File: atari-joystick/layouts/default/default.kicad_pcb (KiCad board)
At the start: 2 copper layers, 31.5 x 30 mm, 19 parts

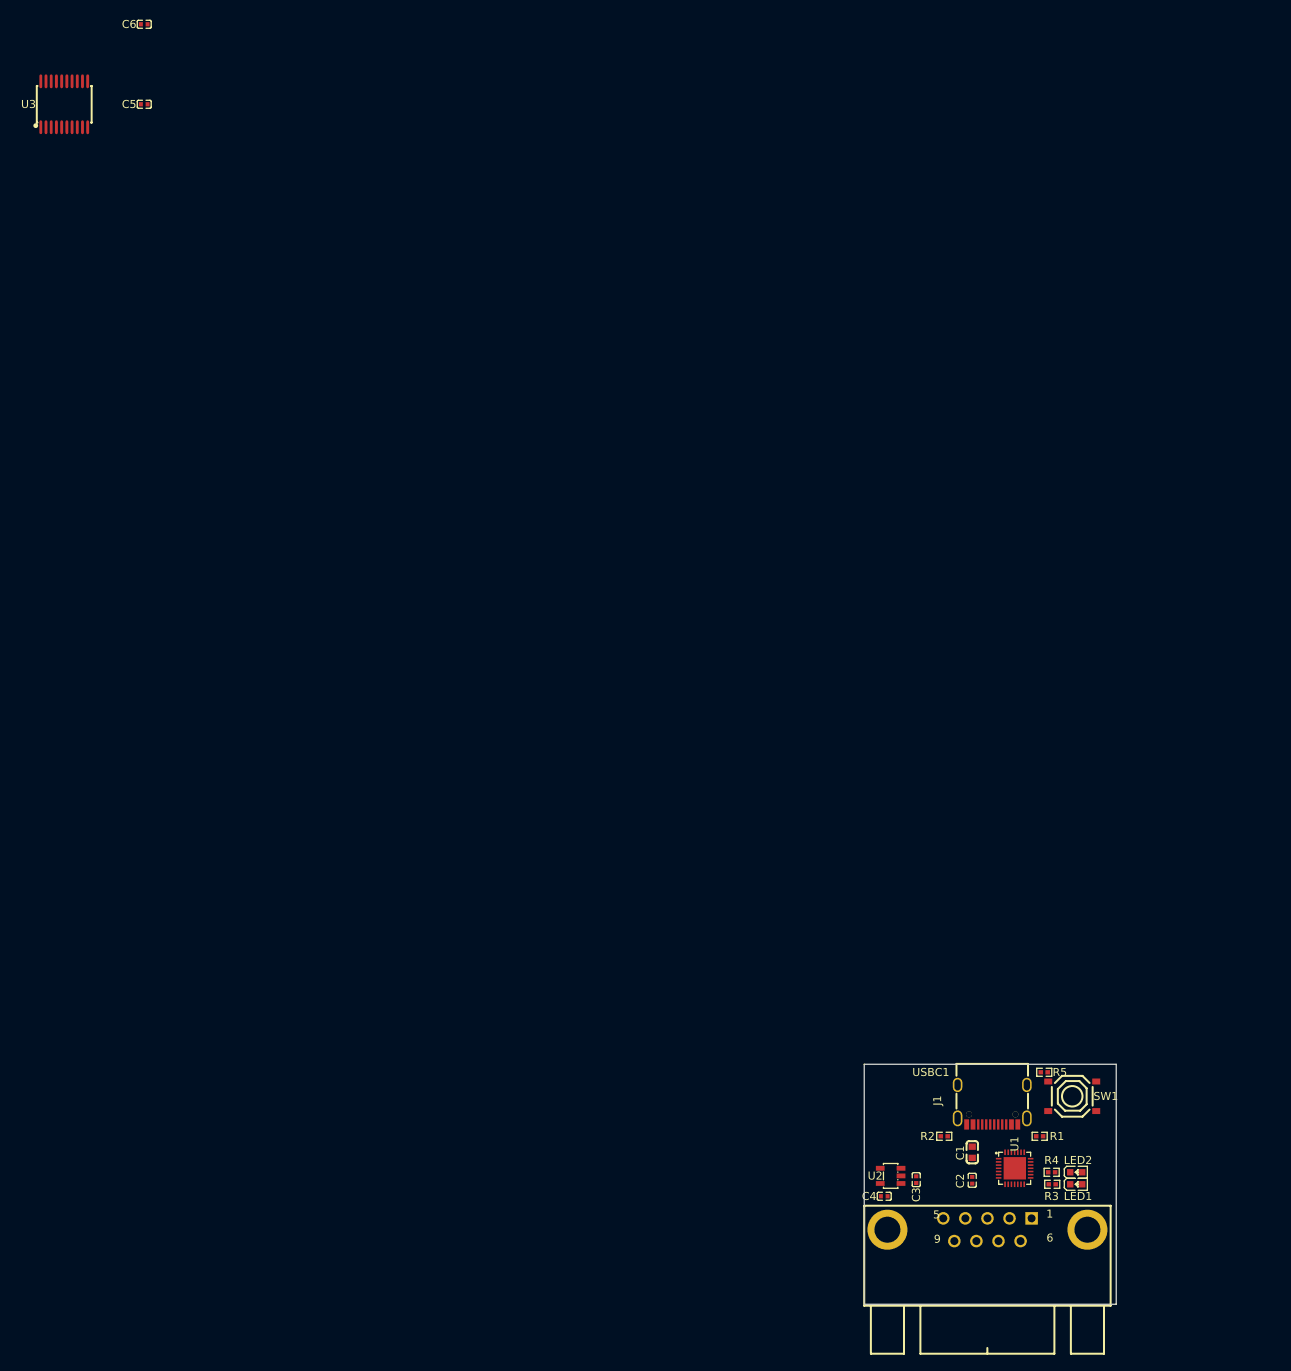
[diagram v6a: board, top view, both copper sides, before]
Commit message: atari-joystick: x68000-keyboard の改修を取り込み (LED 削除 / SW / フットプリント)
x68000-keyboard と同じ方針でジョイスティック基板も以下に揃える:

- デバッグ LED (LED0/LED1) と直列抵抗を削除。PB11 / PB12 は未使用化
- BOOT ボタンを XKB TS-1187A (4 ピン 5.1×5.1mm) から
  XUNPU TS-1088-AR02016 (2 ピン 3.9×3.0mm) に変更
- USB-C コネクタのシルク線幅を 0.25mm → 0.2mm に調整 (DRC 対応)
- TC7MPB9307FT (TSSOP-20) フットプリント整形
- buttons.ato に TactSwitch_2P モジュール追加

SW1 のピン数変更で発生する atopile のフットプリント差し替えバグ
(unmatched-pads ログ整形クラッシュ) は、PCB から既存 J1/SW1 ブロックを
事前に取り除いてから再ビルドして回避。その他のレイアウト配置は保持。

Co-Authored-By: Claude Opus 4.7 (1M context) <noreply@anthropic.com>
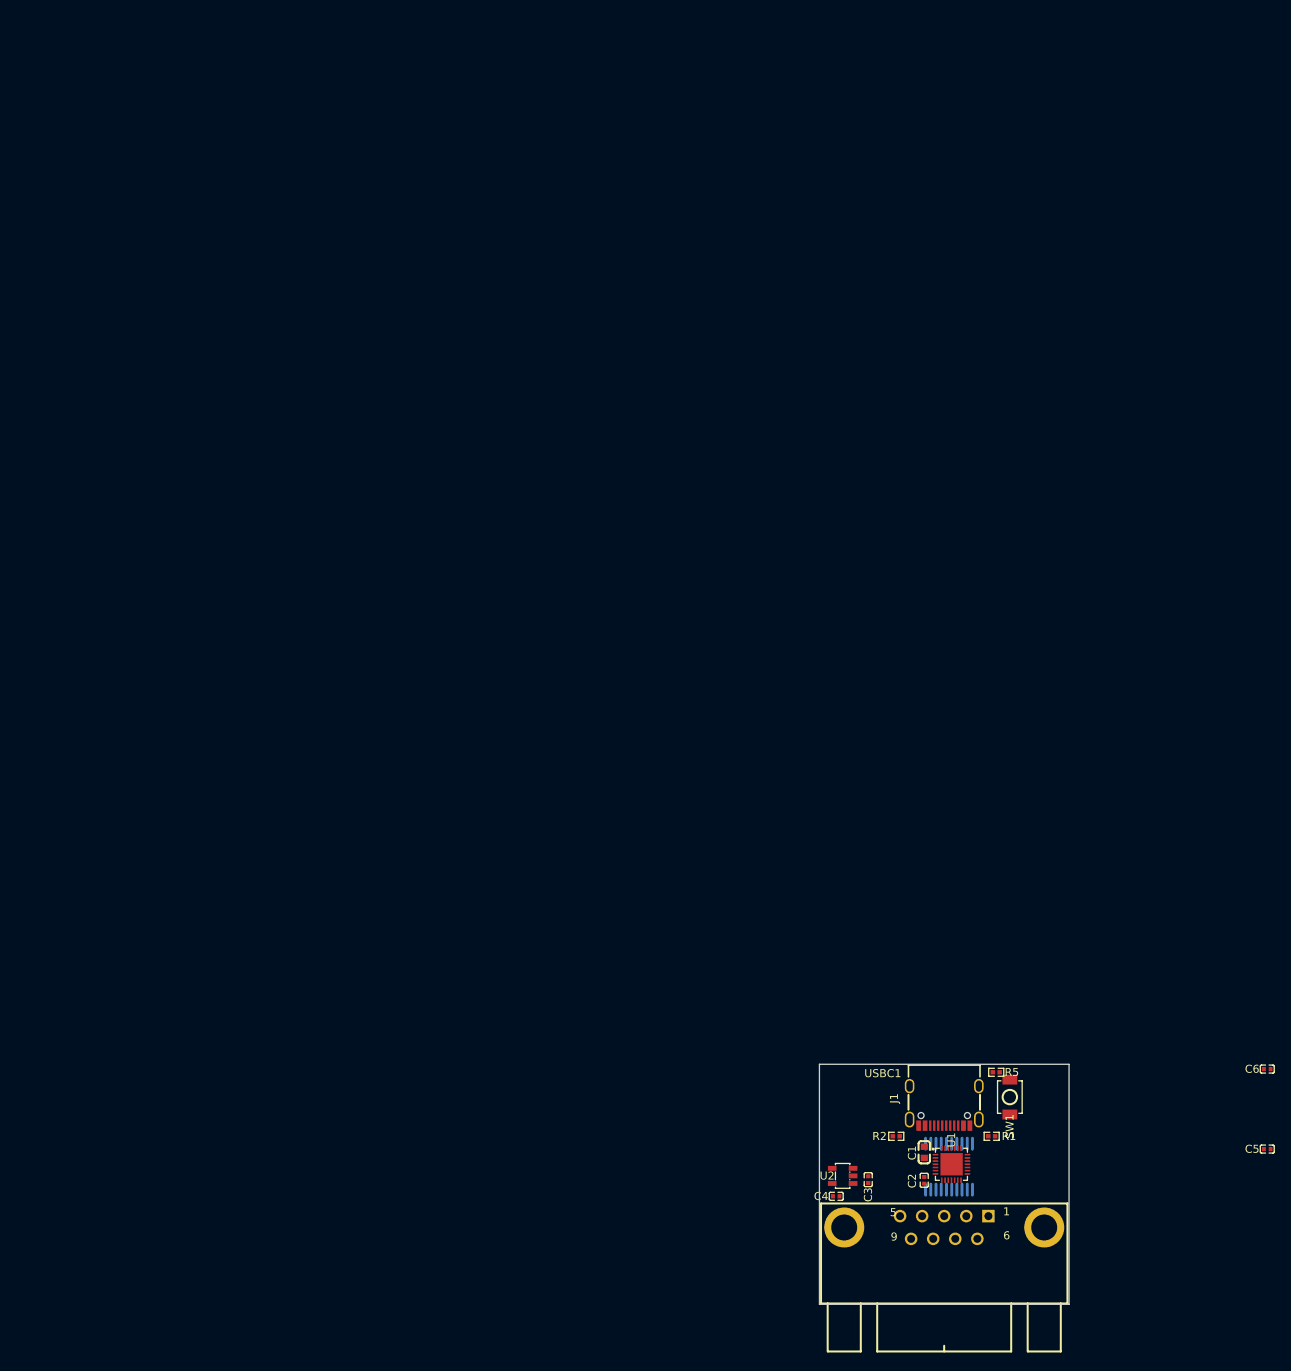
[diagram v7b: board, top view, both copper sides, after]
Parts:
- removed LED1: , Everlight_Elec_19_217_GHC_YR1S2_3T:LED0603-RD
- removed LED2: , Hubei_KENTO_Elec_KT_0603R:LED0603-RD
- removed R3, R4: 470Ω ±1%, UNI_ROYAL_0402WGF4700TCE:R0402
- SW1: footprint XKB_Connectivity_TS_1187A_B_A_B:SW-SMD_4P-L5.1-W5.1-P3.70-LS6.5-TL_H1.5 -> XUNPU_TS_1088_AR02016:SW-SMD_L3.9-W3.0-P4.45
- U3: moved to B.Cu
- moved C5 191.7 mm to (150.4, 130.6)
- moved C6 191.7 mm to (150.4, 120.6)
- moved U3 172.8 mm to (110.6, 132.8)
- moved U1 7.92 mm to (110.9, 132.5)
- moved SW1 7.80 mm to (118.2, 124.1), turned to 90 degrees
- moved USBC1 6.00 mm to (110.0, 125.2)
- moved C1 6.00 mm to (107.5, 131.0)
- moved C2 6.00 mm to (107.5, 134.5)
- moved C3 6.00 mm to (100.5, 134.4)
- moved C4 6.00 mm to (96.5, 136.5)
- moved R1 6.00 mm to (115.9, 129.0)
- moved R2 6.00 mm to (104.0, 129.0)
- moved R5 6.00 mm to (116.5, 121.0)
- moved U2 6.00 mm to (97.3, 133.9)
- moved J1 5.41 mm to (110.0, 140.4)
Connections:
- SW1 pad 2: VDD33 -> terminal_b
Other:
- board size 31.5 x 30 mm -> 31.2 x 30 mm

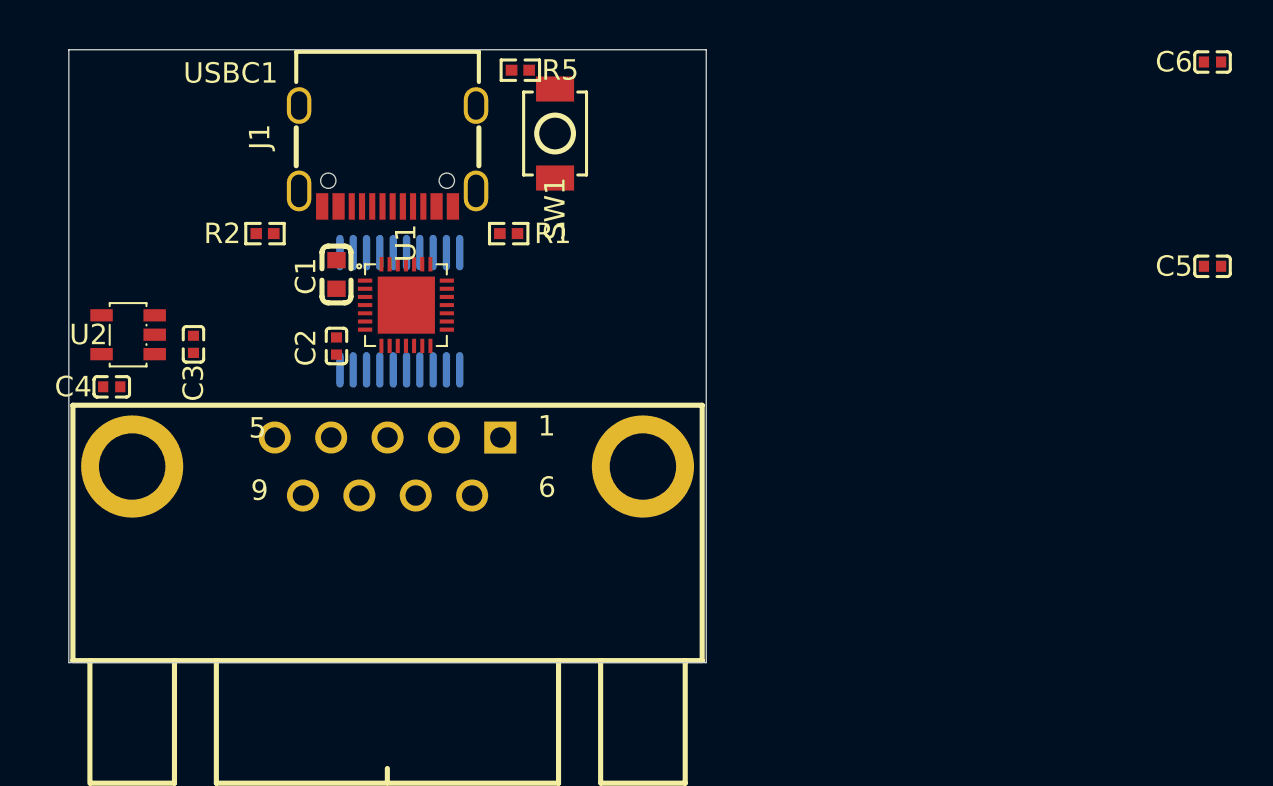
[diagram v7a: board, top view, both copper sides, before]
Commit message: atari-joystick: USB-C シェルを GND に接続、レベルシフタ割当を配線優先で見直し
x68000-keyboard と同様、USB Type-C コネクタのシェル / 機構フレーム端子を
GND ネット (vbus.lv) に直結。シールド経由のリターンパスとシャーシ電位を
0V に固定する。

あわせて、レベルシフタの a1〜a7 割当を a8/a6/a4/a2/a7/a5/a3 に再配置し、
予備チャネルを Ch.1 (旧 Ch.8) に変更。PCB レイアウト上の配線取り回しを
優先した結果。

Co-Authored-By: Claude Opus 4.7 (1M context) <noreply@anthropic.com>
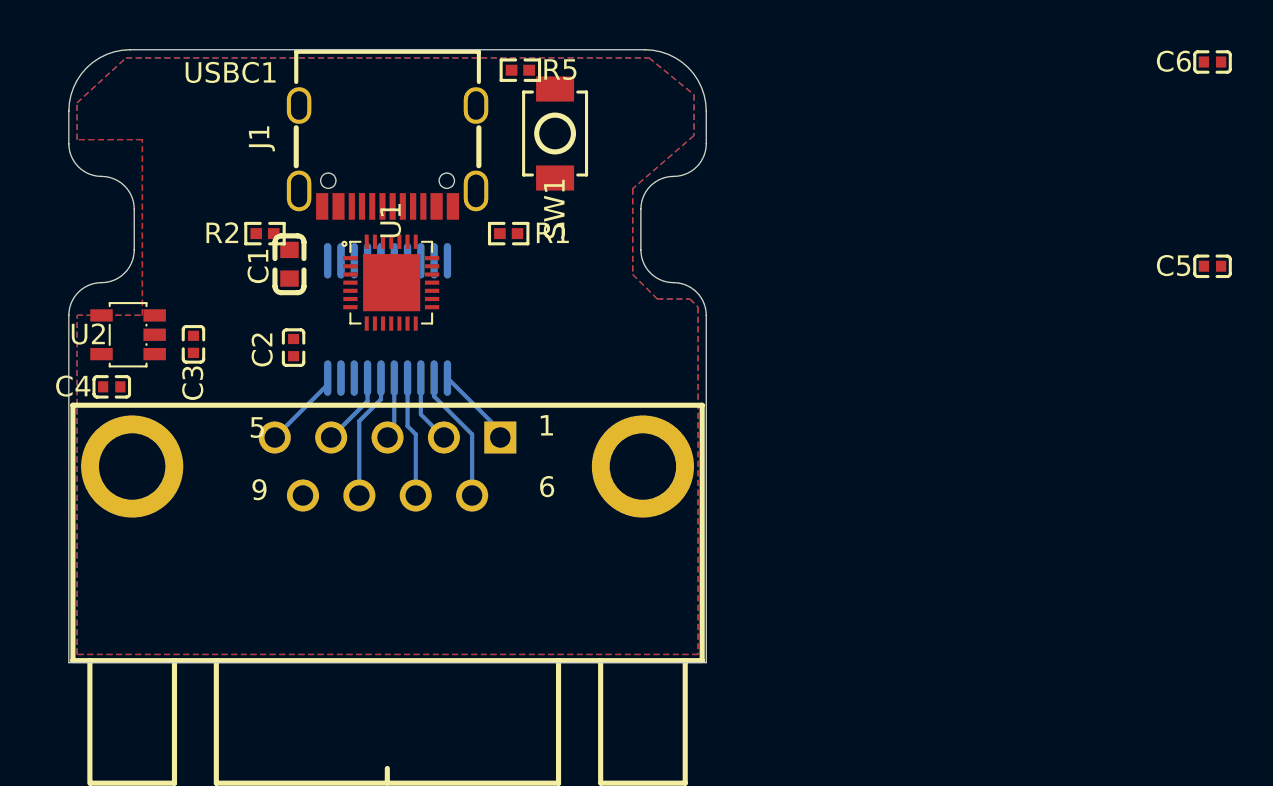
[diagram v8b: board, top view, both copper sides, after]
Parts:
- moved C1 2.35 mm to (105.2, 130.5)
- moved C2 2.10 mm to (105.4, 134.6)
- moved U1 1.31 mm to (110.2, 131.4)
- moved U3 0.72 mm to (110.0, 133.2)
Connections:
- U3 pad 11: b8 -> up
- U3 pad 12: common -> triga
- U3 pad 13: trigb -> down
- U3 pad 14: triga -> trigb
- U3 pad 15: right -> left
- U3 pad 16: left -> common
- U3 pad 17: down -> right
- U3 pad 18: up -> b1
- U3 pad 2: UP_3V3 -> GND
- U3 pad 3: DOWN_3V3 -> RIGHT_3V3
- U3 pad 4: LEFT_3V3 -> COMMON_3V3
- U3 pad 5: RIGHT_3V3 -> LEFT_3V3
- U3 pad 6: TRIGA_3V3 -> TRIGB_3V3
- U3 pad 7: TRIGB_3V3 -> DOWN_3V3
- U3 pad 8: COMMON_3V3 -> TRIGA_3V3
- U3 pad 9: GND -> UP_3V3
- USBC1 pad 1: usbc-shell -> GND
- USBC1 pad 2: usbc-shell -> GND
- USBC1 pad 3: usbc-shell -> GND
- USBC1 pad 4: usbc-shell -> GND
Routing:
- net triga: track 0.00 -> 6.52 mm
- net common: track 0.00 -> 6.19 mm
- net trigb: track 0.00 -> 5.92 mm
- net up: track 0.00 -> 3.98 mm
- net VCC_HOST: track 0.00 -> 3.98 mm
- net right: track 0.00 -> 3.65 mm
- net down: track 0.00 -> 3.38 mm
- net left: track 0.00 -> 3.05 mm
- added copper zone on B.Cu, net GND
- added copper zone on F.Cu, net GND
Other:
- outline, holes or cut-outs redrawn
